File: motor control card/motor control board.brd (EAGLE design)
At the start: 100 x 80 mm, 18 parts, among them J1 09231486921, J2 TBP02R1-381-07BE, J3 TBP02R1-381-07BE

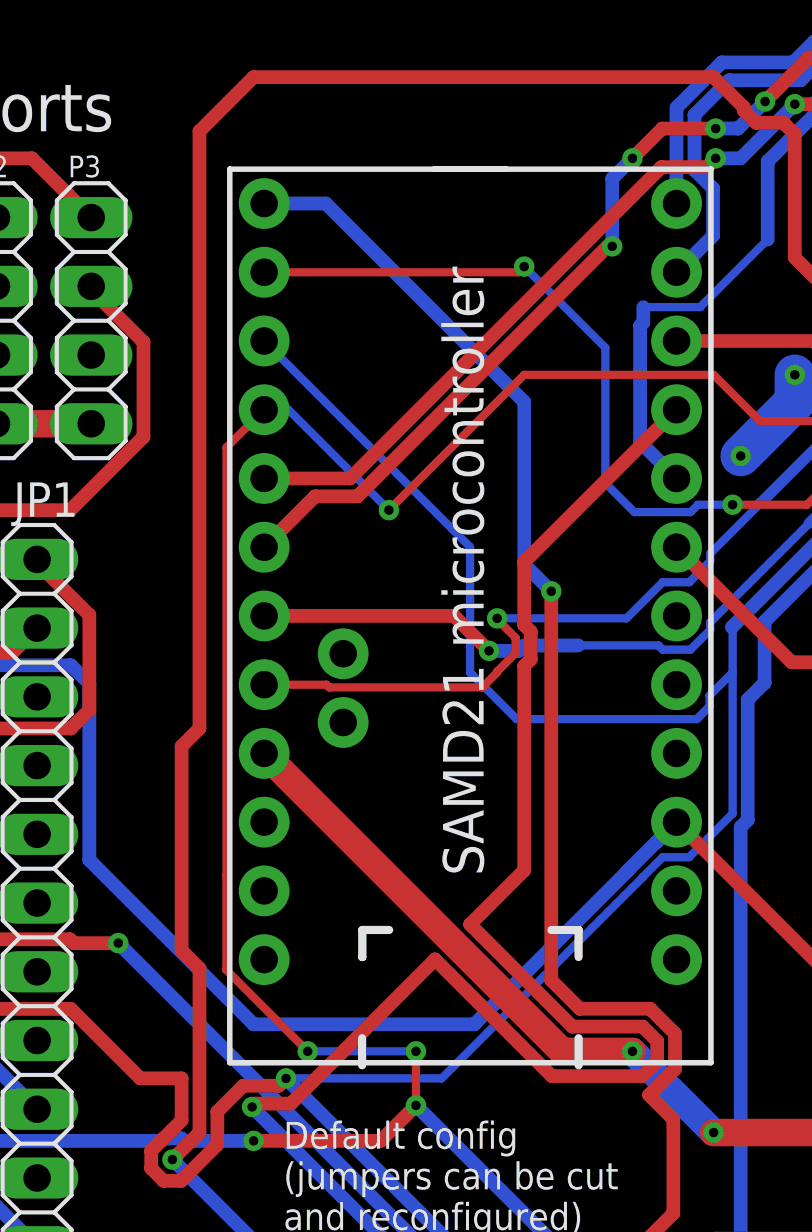
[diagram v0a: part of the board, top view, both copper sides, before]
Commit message: updated libraries to generate better bom's
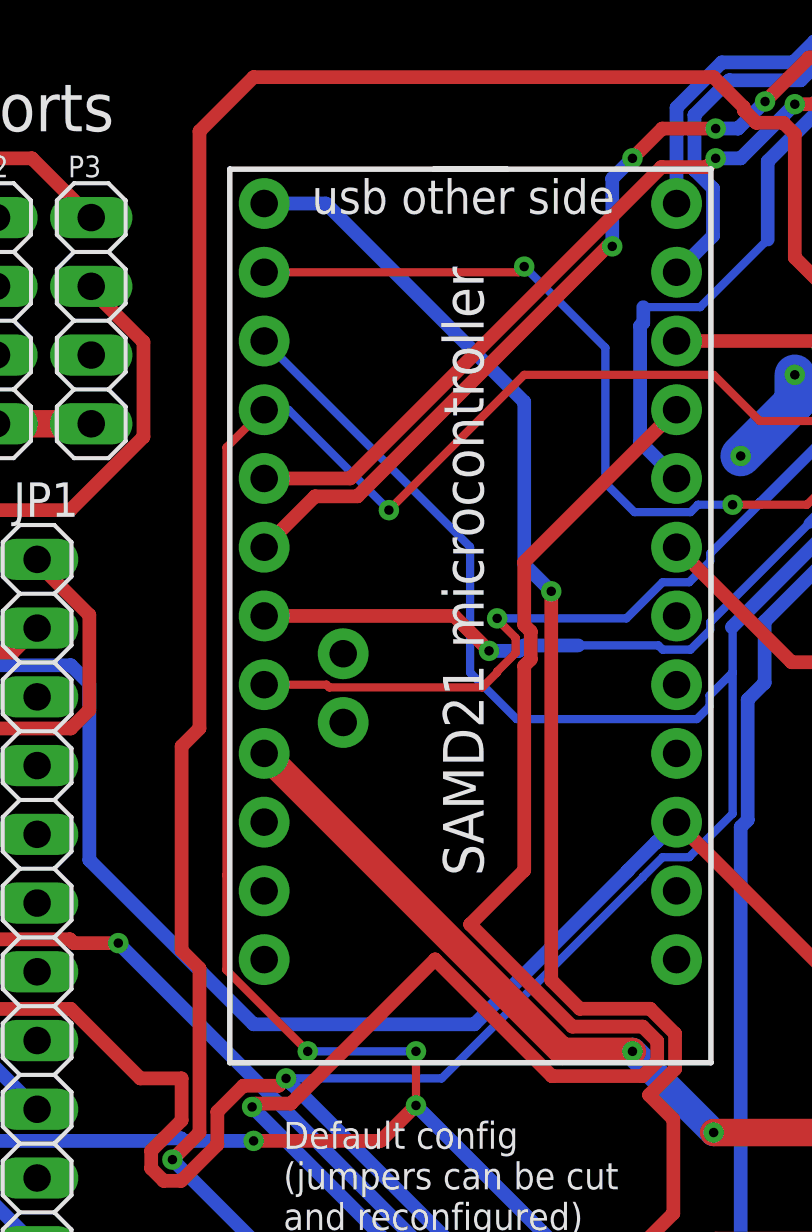
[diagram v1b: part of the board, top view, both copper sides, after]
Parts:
- U$4: value (none) -> SAM_D21_MINI_BREAKOUT
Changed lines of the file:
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@@
 </autorouter>
 <elements>
-<element name="J1" library="din41612_48_pin_board" package="HARTING_09231486921" value="09231486921" x="5.6" y="20.95" smashed="yes" rot="R270">
-<attribute name="AVAILABILITY" value="In Stock" x="5.6" y="20.95" size="1.778" layer="27" rot="R270" display="off"/>
-<attribute name="COMMENT" value="09231486921" x="5.6" y="20.95" size="1.778" layer="27" rot="R270" display="off"/>
-<attribute name="DESCRIPTION" value=" Conn DIN 41612 M 48 POS 2.54mm Solder RA Thru-Hole Tray " x="5.6" y="20.95" size="1.778" layer="27" rot="R270" display="off"/>
-<attribute name="EU_ROHS_COMPLIANCE" value="Compliant" x="5.6" y="20.95" size="1.778" layer="27" rot="R270" display="off"/>
-<attribute name="MF" value="HARTING" x="5.6" y="20.95" size="1.778" layer="27" rot="R270" display="off"/>
-<attribute name="MP" value="09231486921" x="5.6" y="20.95" size="1.778" layer="27" rot="R270" display="off"/>
+<element name="J1" library="din41612_48_pin_board" package="HARTING_09231486921" package3d_urn="urn:adsk.eagle:package:31078162/1" value="09231486921" x="5.6" y="20.95" smashed="yes" rot="R270">
+<attribute name="MANUFACTURER-PART-NUMBER" value="09231486921" x="5.6" y="20.95" size="1.778" layer="27" rot="R270" display="off"/>
 <attribute name="NAME" x="3.505" y="67.18" size="1.27" layer="25"/>
 <attribute name="PACKAGE" value="None" x="5.6" y="20.95" size="1.778" layer="27" rot="R270" display="off"/>
-<attribute name="PRICE" value="6$" x="5.6" y="20.95" size="1.778" layer="27" rot="R270" display="off"/>
-<attribute name="PURCHASE-URL-DIGIKEY" value="https://www.digikey.ca/en/products/detail/harting/09231486921/3180439" x="5.6" y="20.95" size="1.778" layer="27" rot="R270" display="off"/>
+<attribute name="SIMILAR-COMPONENTS" value="" x="5.6" y="20.95" size="1.778" layer="27" rot="R270" display="off"/>
 <attribute name="VALUE" x="-8.59" y="67.68" size="1.27" layer="27" rot="R270"/>
 </element>
@@
 <attribute name="VALUE" x="32.03" y="17.625" size="1.27" layer="27"/>
 </element>
-<element name="SJ1" library="SparkFun-Passives" package="SJ_2S-TRACE" value="SOLDERJUMPERTRACE" x="30" y="25" smashed="yes">
+<element name="SJ1" library="SparkFun-Passives" package="SJ_2S-TRACE" package3d_urn="urn:adsk.eagle:package:30824525/1" value="SOLDERJUMPERTRACE" x="30" y="25" smashed="yes">
 <attribute name="NAME" x="29.0475" y="26.27" size="0.4064" layer="25"/>
 <attribute name="VALUE" x="29.0475" y="23.349" size="0.4064" layer="27"/>
 </element>
-<element name="SJ2" library="SparkFun-Passives" package="SJ_2S-TRACE" value="SOLDERJUMPERTRACE" x="30" y="21" smashed="yes" rot="R180">
+<element name="SJ2" library="SparkFun-Passives" package="SJ_2S-TRACE" package3d_urn="urn:adsk.eagle:package:30824525/1" value="SOLDERJUMPERTRACE" x="30" y="21" smashed="yes" rot="R180">
 <attribute name="NAME" x="30.9525" y="19.73" size="0.4064" layer="25" rot="R180"/>
 <attribute name="VALUE" x="35.4525" y="22.651" size="0.4064" layer="27" rot="R180"/>
@@
 <attribute name="VALUE" x="32.03" y="26.125" size="1.27" layer="27"/>
 </element>
-<element name="SJ3" library="SparkFun-Passives" package="SJ_2S-TRACE" value="SOLDERJUMPERTRACE" x="30" y="29" smashed="yes">
+<element name="SJ3" library="SparkFun-Passives" package="SJ_2S-TRACE" package3d_urn="urn:adsk.eagle:package:30824525/1" value="SOLDERJUMPERTRACE" x="30" y="29" smashed="yes">
 <attribute name="NAME" x="29.0475" y="30.27" size="0.4064" layer="25"/>
 <attribute name="VALUE" x="29.0475" y="27.349" size="0.4064" layer="27"/>
@@
 <attribute name="PURCHASE-URL" value="https://pricing.snapeda.com/search/part/TBP02R1-381-07BE/?ref=eda" x="95" y="66.86" size="1.778" layer="27" rot="R270" display="off"/>
 </element>
-<element name="SJ4" library="SparkFun-Passives" package="SJ_2S-TRACE" value="SOLDERJUMPERTRACE" x="57" y="34" smashed="yes">
+<element name="SJ4" library="SparkFun-Passives" package="SJ_2S-TRACE" package3d_urn="urn:adsk.eagle:package:30824525/1" value="SOLDERJUMPERTRACE" x="57" y="34" smashed="yes">
 <attribute name="NAME" x="56.0475" y="35.27" size="0.4064" layer="25"/>
 </element>
-<element name="SJ5" library="SparkFun-Passives" package="SJ_2S-TRACE" value="SOLDERJUMPERTRACE" x="56" y="69" smashed="yes">
+<element name="SJ5" library="SparkFun-Passives" package="SJ_2S-TRACE" package3d_urn="urn:adsk.eagle:package:30824525/1" value="SOLDERJUMPERTRACE" x="56" y="69" smashed="yes">
 <attribute name="NAME" x="55.0475" y="70.27" size="0.4064" layer="25"/>
 </element>
-<element name="U$4" library="SparkFun-SAMD21-Mini-Breakout" package="JP1_SPARKFUN-SAMD21-MINI-BREAKOUT-V10" value="" x="46.9" y="71.6" smashed="yes" rot="R180">
-<attribute name="PURCHASE_URL_DIGIKEY" value="https://www.digikey.ca/en/products/detail/sparkfun-electronics/DEV-13664/5766914?s=N4IgTCBcDaIM4EMC2ATMBGABEglgOx0wCMAnAUwQGsB7AVwBcQBdAXyA" x="46.9" y="71.6" size="1.778" layer="27" rot="R180" display="off"/>
-<attribute name="PURCHASE_URL_SPARKFUN" value="https://www.sparkfun.com/products/13664" x="46.9" y="71.6" size="1.778" layer="27" rot="R180" display="off"/>
+<element name="U$4" library="SparkFun-SAMD21-Mini-Breakout" package="JP1_SPARKFUN-SAMD21-MINI-BREAKOUT-V10" value="SAM_D21_MINI_BREAKOUT" x="46.9" y="71.6" smashed="yes" rot="R180">
+<attribute name="MANUFACTURER-PART-NUMBE" value="SparkFun SAMD21 mini breakout, SLW-112-01-G-S  &lt; buy two of these" x="46.9" y="71.6" size="1.778" layer="27" rot="R180" display="off"/>
+<attribute name="PACKAGE" value="None" x="46.9" y="71.6" size="1.778" layer="27" rot="R180" display="off"/>
+<attribute name="SIMILAR-COMPONENTS" value="None, https://www.adafruit.com/product/3008" x="46.9" y="71.6" size="1.778" layer="27" rot="R180" display="off"/>
 </element>
 <element name="JP5" library="pinhead" library_urn="urn:adsk.eagle:library:325" package="1X04" package3d_urn="urn:adsk.eagle:package:22407/2" value="" x="17" y="66" smashed="yes" rot="R90">
@@
 <contactref element="JP6" pad="2"/>
 <contactref element="JP7" pad="2"/>
+<wire x1="82.73" y1="58.49" x2="95" y2="59.24" width="0" layer="19" extent="1-1"/>
+<wire x1="82.73" y1="55.95" x2="82.73" y2="58.49" width="0" layer="19" extent="1-1"/>
+<wire x1="57" y1="51" x2="82.73" y2="55.95" width="0" layer="19" extent="1-1"/>
+<wire x1="45.63" y1="50.01" x2="52.25" y2="50.84" width="0" layer="19" extent="1-1"/>
+<wire x1="48" y1="61" x2="52.25" y2="50.84" width="0" layer="19" extent="1-1"/>
+<wire x1="24" y1="64.73" x2="48" y2="61" width="0" layer="19" extent="1-1"/>
+<wire x1="20.5" y1="64.73" x2="24" y2="64.73" width="0" layer="19" extent="1-1"/>
+<wire x1="17" y1="64.73" x2="20.5" y2="64.73" width="0" layer="19" extent="1-1"/>
+<wire x1="95" y1="28.38" x2="82.73" y2="55.95" width="0" layer="19" extent="1-1"/>
+<wire x1="82.73" y1="24.49" x2="95" y2="28.38" width="0" layer="19" extent="1-1"/>
+<wire x1="82.73" y1="21.95" x2="82.73" y2="24.49" width="0" layer="19" extent="1-1"/>
+<wire x1="52.25" y1="16.84" x2="82.73" y2="21.95" width="0" layer="19" extent="1-1"/>
+<wire x1="42.6" y1="14.8" x2="52.25" y2="16.84" width="0" layer="19" extent="1-1"/>
+<wire x1="42" y1="14" x2="42.6" y2="14.8" width="0" layer="19" extent="1-1"/>
+<wire x1="40.1" y1="18.4" x2="40.1" y2="19.3" width="0" layer="19" extent="1-1"/>
+<wire x1="40.9" y1="18.8" x2="40.1" y2="18.4" width="0" layer="19" extent="1-1"/>
+<wire x1="41.5" y1="14.8" x2="42" y2="14" width="0" layer="19" extent="1-1"/>
+<wire x1="10.68" y1="20.95" x2="40.1" y2="19.3" width="0" layer="19" extent="1-1"/>
+<wire x1="10.68" y1="23.49" x2="10.68" y2="20.95" width="0" layer="19" extent="1-1"/>
+<wire x1="10.68" y1="26.03" x2="10.68" y2="23.49" width="0" layer="19" extent="1-1"/>
+<wire x1="8.14" y1="26.03" x2="10.68" y2="26.03" width="0" layer="19" extent="1-1"/>
+<wire x1="5.6" y1="26.03" x2="8.14" y2="26.03" width="0" layer="19" extent="1-1"/>
+<wire x1="5.6" y1="28.57" x2="5.6" y2="26.03" width="0" layer="19" extent="1-1"/>
+<wire x1="8.14" y1="23.49" x2="10.68" y2="23.49" width="0" layer="19" extent="1-1"/>
+<wire x1="5.6" y1="23.49" x2="5.6" y2="26.03" width="0" layer="19" extent="1-1"/>
+<wire x1="8.14" y1="20.95" x2="10.68" y2="20.95" width="0" layer="19" extent="1-1"/>
+<wire x1="5.6" y1="20.95" x2="5.6" y2="23.49" width="0" layer="19" extent="1-1"/>
 </signal>
 <signal name="24V/12V">
@@
 <vertex x="5.199996875" y="34.5"/>
 </polygon>
+<wire x1="82.73" y1="50.87" x2="82.73" y2="53.41" width="0" layer="19" extent="1-1"/>
+<wire x1="82.73" y1="19.41" x2="82.73" y2="50.87" width="0" layer="19" extent="1-1"/>
+<wire x1="82.73" y1="16.87" x2="82.73" y2="19.41" width="0" layer="19" extent="1-1"/>
+<wire x1="10.68" y1="28.57" x2="82.73" y2="19.41" width="0" layer="19" extent="1-1"/>
+<wire x1="10.68" y1="31.11" x2="10.68" y2="28.57" width="0" layer="19" extent="1-1"/>
+<wire x1="8.14" y1="31.11" x2="10.68" y2="31.11" width="0" layer="19" extent="1-1"/>
+<wire x1="8.14" y1="33.65" x2="8.14" y2="31.11" width="0" layer="19" extent="1-1"/>
+<wire x1="5.6" y1="33.65" x2="8.14" y2="33.65" width="0" layer="19" extent="1-1"/>
+<wire x1="5.6" y1="31.11" x2="8.14" y2="31.11" width="0" layer="19" extent="1-1"/>
+<wire x1="8.14" y1="28.57" x2="10.68" y2="28.57" width="0" layer="19" extent="1-1"/>
 </signal>
 <signal name="5V">
